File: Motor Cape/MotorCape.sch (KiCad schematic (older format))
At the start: 13 parts, among them J1 Conn_01x06, J2 Conn_01x06, J3 Conn_01x06, J4 Conn_01x06, J5 Conn_01x06, J6 Conn_01x06, J7 Conn_01x02, J8 Servo1, J9 Servo2, U1 MotorControl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

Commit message: Worked on wiring motor cape connections.
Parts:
- removed J5, J6: Conn_01x06, symbol Conn_01x06
- removed U3: MotorControl, symbol MotorControl
- added J5: Servo 3, symbol Conn_01x03
- added J6: Servo 4, symbol Conn_01x03
- J1: value Conn_01x06 -> Front Motor 1
- J2: value Conn_01x06 -> Front Motor 2
- J3: value Conn_01x06 -> Back Motor 1
- J4: value Conn_01x06 -> Back Motor 2
- J8: value Servo1 -> Servo 1
- J9: value Servo2 -> Servo 2
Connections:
- net labels added: GND
- net labels removed: +3.3V
- wire segments 36 -> 93
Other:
- moved on the sheet: J2, J3, J4, J7, J8, J9

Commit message: Changes made during meeting
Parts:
- removed J5: Servo 3, symbol Conn_01x03
- removed J6: Servo 4, symbol Conn_01x03
- removed U8: BoneHeaderP8, symbol BoneHeaderP8
- added ARD1: Arduino_Due_Shield, symbol Arduino_Due_Shield
- added J10: Servo2, Pin_Headers:Pin_Header_Angled_1x03_Pitch2.54mm, symbol Conn_01x03
- added J11: Servo1, Pin_Headers:Pin_Header_Angled_1x03_Pitch2.54mm, symbol Conn_01x03
- added J5, J6: Conn_01x06, Pin_Headers:Pin_Header_Angled_1x06_Pitch2.54mm, symbol Conn_01x06
- added U3: MotorControl, symbol MotorControl
- J1: value Front Motor 1 -> Conn_01x06; footprint (none) -> Pin_Headers:Pin_Header_Angled_1x06_Pitch2.54mm
- J2: value Front Motor 2 -> Conn_01x06; footprint (none) -> Pin_Headers:Pin_Header_Angled_1x06_Pitch2.54mm
- J3: value Back Motor 1 -> Conn_01x06; footprint (none) -> Pin_Headers:Pin_Header_Angled_1x06_Pitch2.54mm
- J4: value Back Motor 2 -> Conn_01x06; footprint (none) -> Pin_Headers:Pin_Header_Angled_1x06_Pitch2.54mm
- J8: value Servo 1 -> Servo4; footprint (none) -> Pin_Headers:Pin_Header_Angled_1x03_Pitch2.54mm
- J9: value Servo 2 -> Servo3; footprint (none) -> Pin_Headers:Pin_Header_Angled_1x03_Pitch2.54mm
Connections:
- net labels added: +3.3V
- net labels removed: GND
- wire segments 93 -> 44
- no-connect marks 10 -> 0
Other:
- note removed: "Quad Encoders\n"
- moved on the sheet: J2, J3, J4, J7, J8, J9

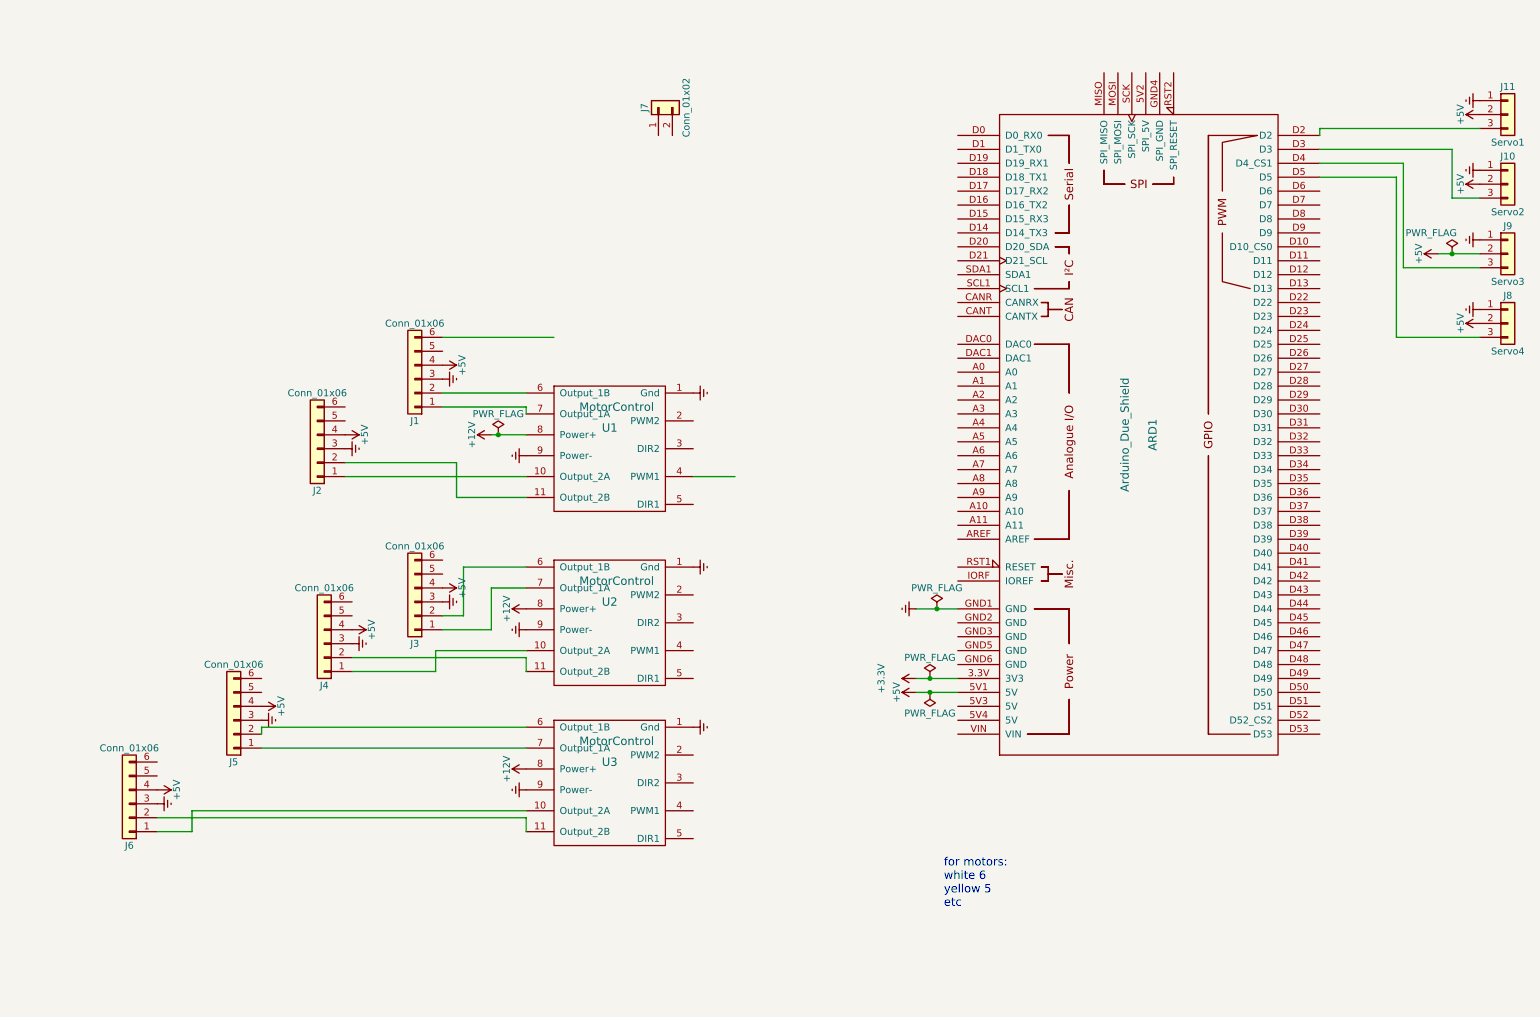
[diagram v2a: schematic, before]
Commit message: updated electrical connections. need to finish connectors on schematic.
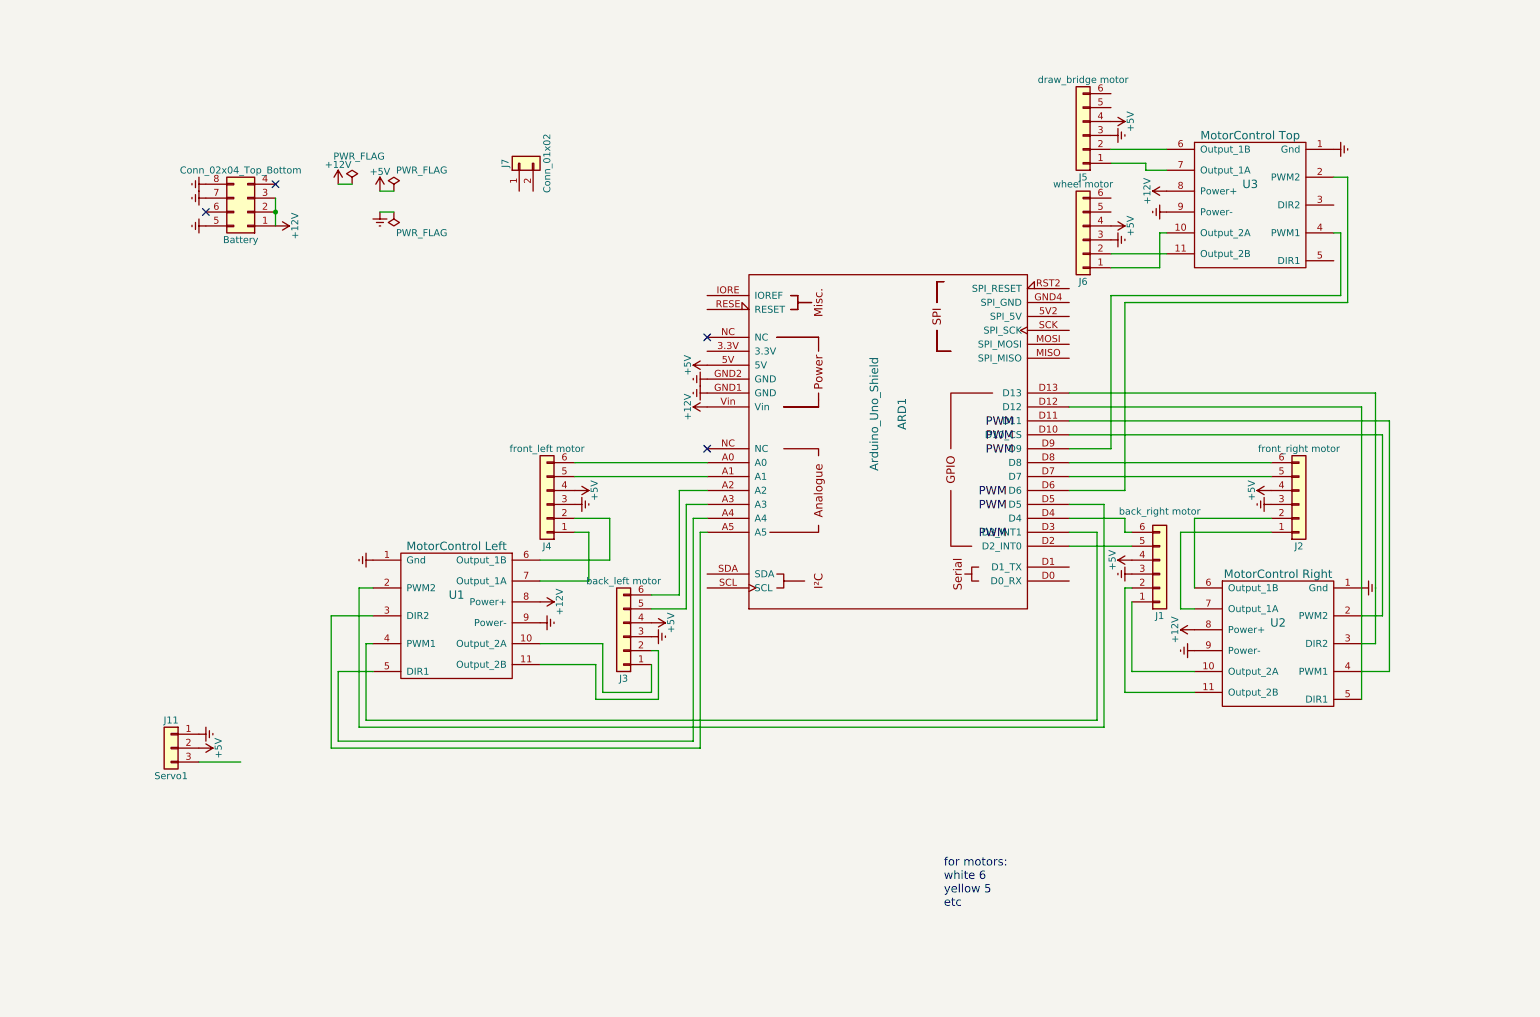
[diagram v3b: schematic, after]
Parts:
- removed ARD1: Arduino_Due_Shield, symbol Arduino_Due_Shield
- removed J10: Servo2, Pin_Headers:Pin_Header_Angled_1x03_Pitch2.54mm, symbol Conn_01x03
- removed J8: Servo4, Pin_Headers:Pin_Header_Angled_1x03_Pitch2.54mm, symbol Conn_01x03
- removed J9: Servo3, Pin_Headers:Pin_Header_Angled_1x03_Pitch2.54mm, symbol Conn_01x03
- added ARD1: Arduino_Uno_Shield, symbol Arduino_Uno_Shield
- added Battery: Conn_02x04_Top_Bottom, symbol Conn_02x04_Top_Bottom
- J1: value Conn_01x06 -> back_right motor
- J2: value Conn_01x06 -> front_right motor
- J3: value Conn_01x06 -> back_left motor
- J4: value Conn_01x06 -> front_left motor
- J5: value Conn_01x06 -> draw_bridge motor
- J6: value Conn_01x06 -> wheel motor
- U1: value MotorControl -> MotorControl Left
- U2: value MotorControl -> MotorControl Right
- U3: value MotorControl -> MotorControl Top
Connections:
- net labels added: PWM
- net labels removed: +3.3V
- wire segments 44 -> 94
- no-connect marks 0 -> 4
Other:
- moved on the sheet: J1, J11, J2, J3, J4, J5, J6, J7, U1, U2, U3

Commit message: updated labels
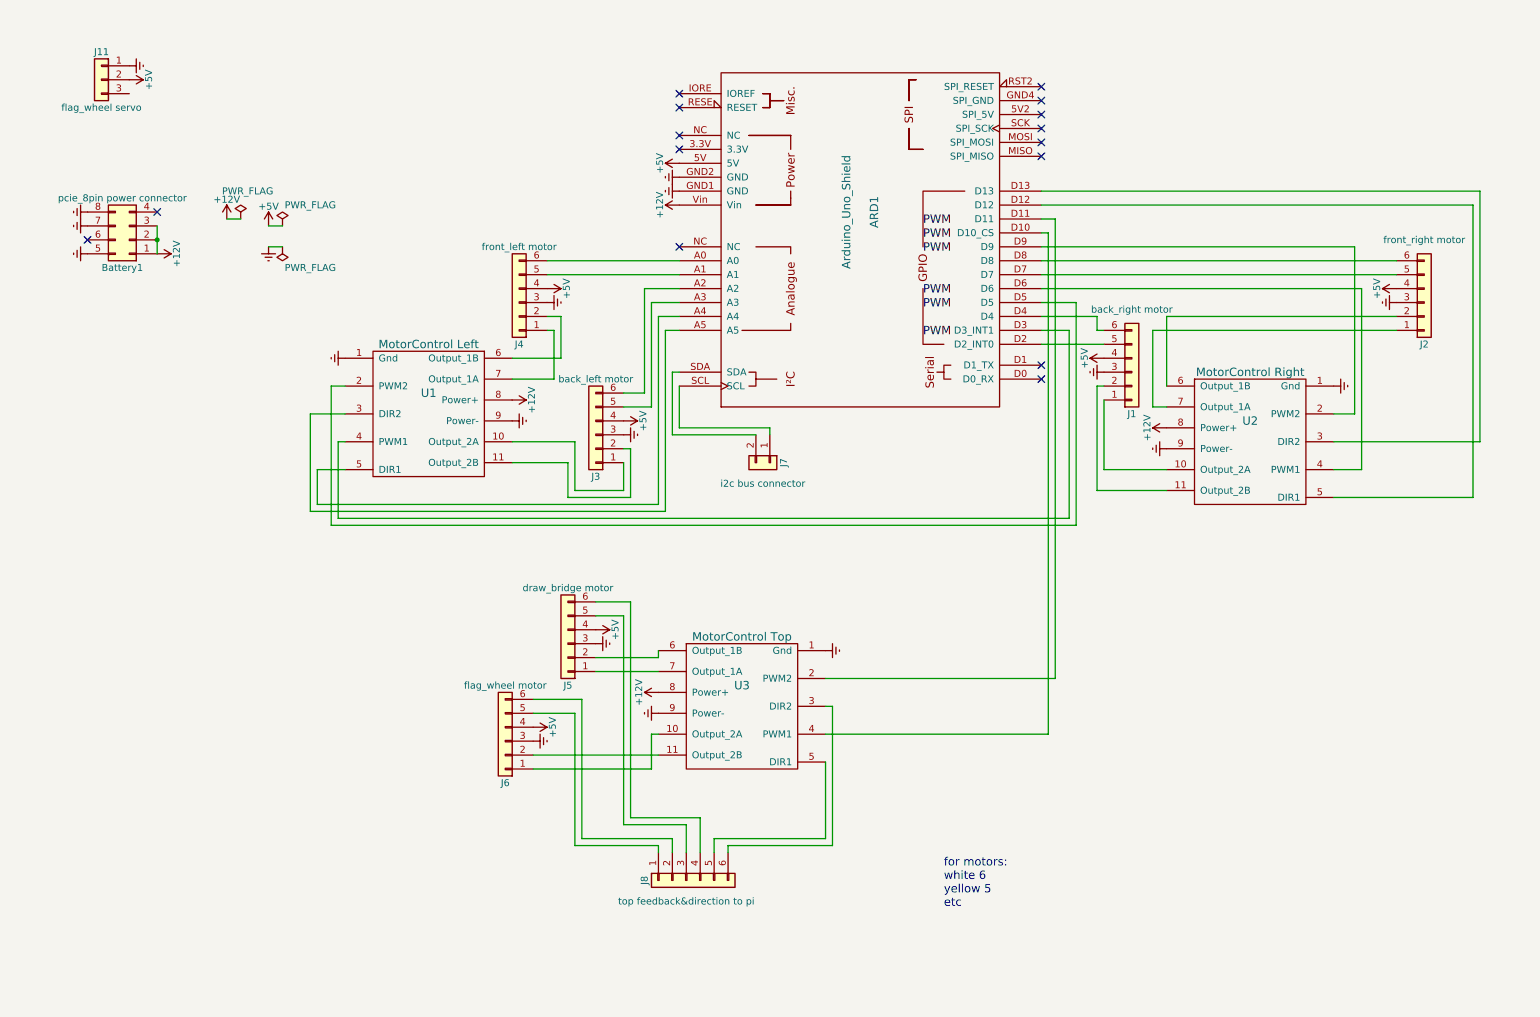
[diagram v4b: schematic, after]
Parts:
- added J8: top feedback&direction to pi, Pin_Headers:Pin_Header_Angled_1x06_Pitch2.54mm, symbol Conn_01x06
- Battery1: renamed from Battery; value Conn_02x04_Top_Bottom -> pcie_8pin power connector
- J11: value Servo1 -> flag_wheel servo
- J6: value wheel motor -> flag_wheel motor
- J7: value Conn_01x02 -> i2c bus connector
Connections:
- net at U2.2 (PWM2): now also ARD1.D9; no longer ARD1.D10 (D10_CS)
- net at U2.4 (PWM1): now also ARD1.D6; no longer ARD1.D11
- net at U3.2 (PWM2): now also ARD1.D11; no longer ARD1.D6
- net at U3.3 (DIR2): now also J8.6 (Pin_6)
- net at U3.4 (PWM1): now also ARD1.D10 (D10_CS); no longer ARD1.D9
- net at U3.5 (DIR1): now also J8.5 (Pin_5)
- net at J6.5 (Pin_5): now also J8.1 (Pin_1)
- net at J6.6 (Pin_6): now also J8.2 (Pin_2)
- net at J5.5 (Pin_5): now also J8.3 (Pin_3)
- net at J5.6 (Pin_6): now also J8.4 (Pin_4)
- net at J7.1 (Pin_1): now also ARD1.SCL
- net at J7.2 (Pin_2): now also ARD1.SDA
- no-connect marks 4 -> 15
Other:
- moved on the sheet: ARD1, Battery1, J1, J11, J2, J3, J4, J5, J6, J7, U1, U2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

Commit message: added level shifters and due and pi and labels
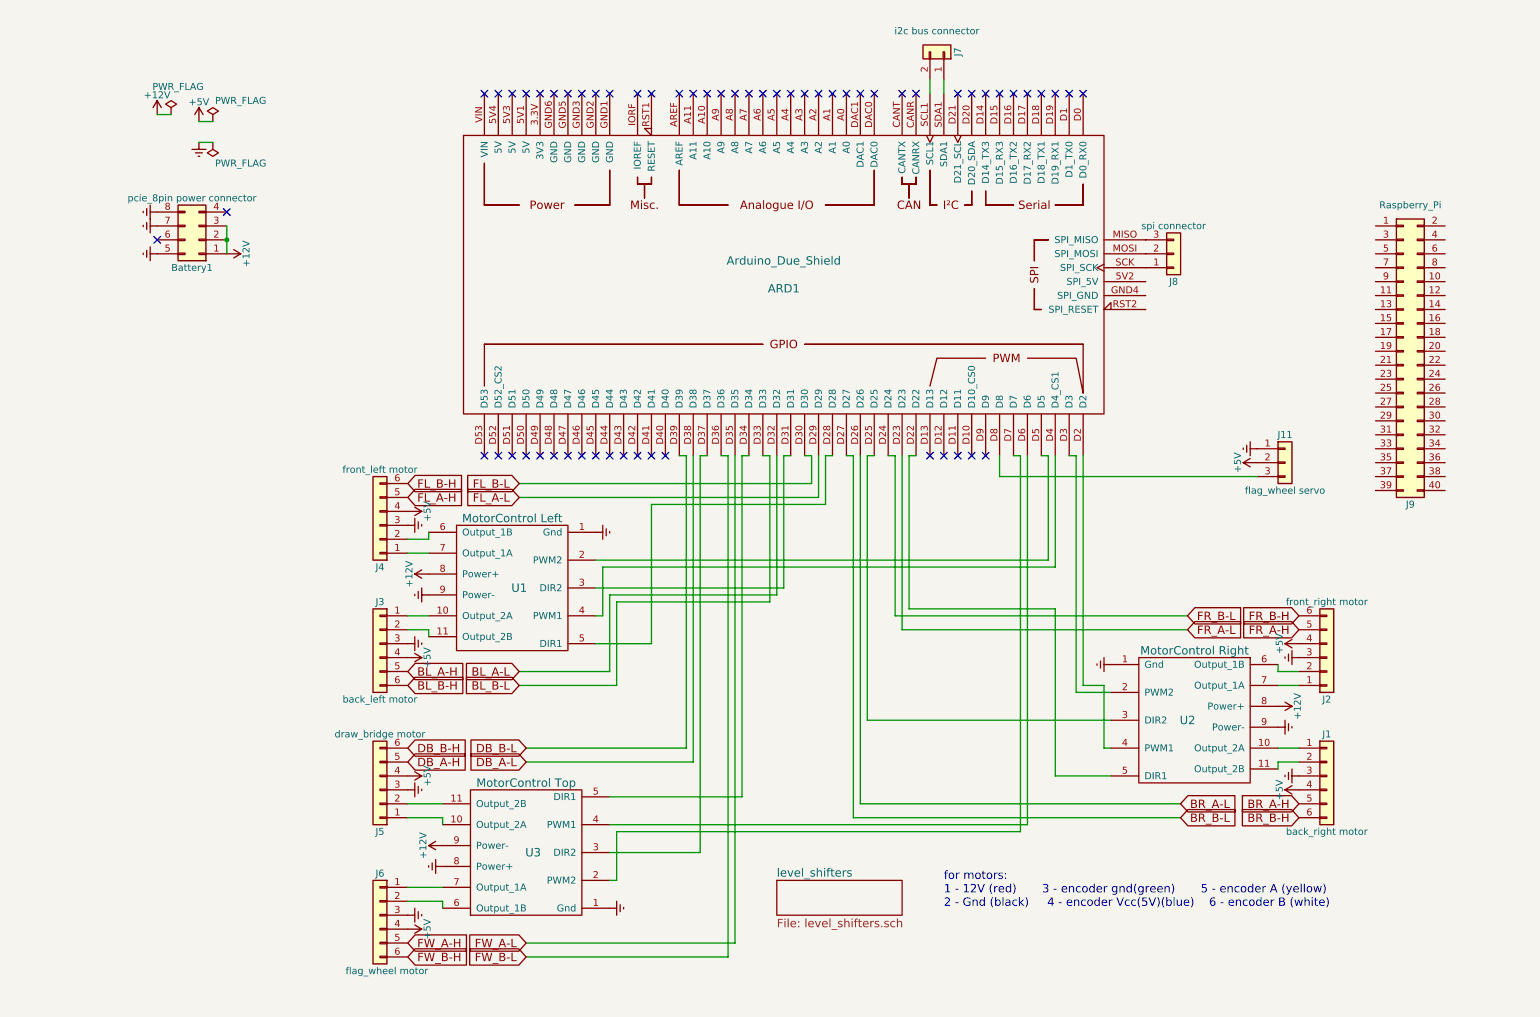
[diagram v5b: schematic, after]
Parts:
- removed ARD1: Arduino_Uno_Shield, symbol Arduino_Uno_Shield
- removed J8: top feedback&direction to pi, Pin_Headers:Pin_Header_Angled_1x06_Pitch2.54mm, symbol Conn_01x06
- added ARD1: Arduino_Due_Shield, symbol Arduino_Due_Shield
- added J8: spi connector, symbol Conn_01x03
- added J9: Raspberry_Pi, symbol Conn_02x20_Odd_Even
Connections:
- net +12V: now also U3.9 (Power-); no longer U3.8 (Power+)
- net Earth: now also U3.8 (Power+); no longer U3.9 (Power-)
- net at U2.2 (PWM2): now also ARD1.D3
- net at U2.3 (DIR2): now also ARD1.D25
- net at U2.4 (PWM1): now also ARD1.D2
- net at U2.5 (DIR1): now also ARD1.D22
- net at U1.2 (PWM2): now also ARD1.D5
- net at U1.3 (DIR2): now also ARD1.D31
- net at U1.4 (PWM1): now also ARD1.D4 (D4_CS1)
- net at U1.5 (DIR1): now also ARD1.D28
- net at U3.10 (Output_2A): now also J5.1 (Pin_1); no longer J6.1 (Pin_1)
- net at U3.11 (Output_2B): now also J5.2 (Pin_2); no longer J6.2 (Pin_2)
- net at U3.2 (PWM2): now also ARD1.D7
- net at U3.3 (DIR2): now also ARD1.D37
- net at U3.4 (PWM1): now also ARD1.D6
- net at U3.5 (DIR1): now also ARD1.D34
- net at U3.6 (Output_1B): now also J6.2 (Pin_2); no longer J5.2 (Pin_2)
- net at U3.7 (Output_1A): now also J6.1 (Pin_1); no longer J5.1 (Pin_1)
- net BR_A-H: now reaches J1.5 (Pin_5)
- net BR_B-H: now reaches J1.6 (Pin_6)
- net FR_A-H: now reaches J2.5 (Pin_5)
- net FR_B-H: now reaches J2.6 (Pin_6)
- net BL_A-H: now reaches J3.5 (Pin_5)
- net BL_B-H: now reaches J3.6 (Pin_6)
- net FL_A-H: now reaches J4.5 (Pin_5)
- net FL_B-H: now reaches J4.6 (Pin_6)
- net FW_A-H: now reaches J6.5 (Pin_5)
- net FW_B-H: now reaches J6.6 (Pin_6)
- net DB_A-H: now reaches J5.5 (Pin_5)
- net DB_B-H: now reaches J5.6 (Pin_6)
- net at J7.1 (Pin_1): now also ARD1.SDA1
- net at J7.2 (Pin_2): now also ARD1.SCL1
- net at J11.3 (Pin_3): now also ARD1.D8
- new net: ARD1.MISO (SPI_MISO), J8.3 (Pin_3)
- new net: ARD1.MOSI (SPI_MOSI), J8.2 (Pin_2)
- new net: ARD1.SCK (SPI_SCK), J8.1 (Pin_1)
- new net BL_A-L: ARD1.D32
- new net BL_B-L: ARD1.D33
- new net BR_A-L: ARD1.D26
- new net BR_B-L: ARD1.D27
- new net DB_A-L: ARD1.D38
- new net DB_B-L: ARD1.D39
- new net FL_A-L: ARD1.D29
- new net FL_B-L: ARD1.D30
- new net FR_A-L: ARD1.D23
- new net FR_B-L: ARD1.D24
- new net FW_A-L: ARD1.D35
- new net FW_B-L: ARD1.D36
- no-connect marks 15 -> 60
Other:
- note added: "for motors: \n1 - 12V (red) 3 - encoder gnd(green) 5 - encoder A (yellow)\n2 - Gnd (black) 4 - encoder Vcc(5V)(blue) 6 - encoder B (white)\n"
- note removed: "for motors:\nwhite 6\nyellow 5\netc\n"
- moved on the sheet: Battery1, J1, J11, J2, J3, J4, J5, J6, J7, U1, U2, U3

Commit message: fixed drc errors, added serial comm between pi & due, now just need to choose power connector & fuse
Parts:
- removed J8: spi connector, symbol Conn_01x03
- removed J9: Raspberry_Pi, symbol Conn_02x20_Odd_Even
- added F1: Fuse, symbol Fuse
- added J9: Raspberry_Pi_2_3, Pin_Headers:Pin_Header_Straight_2x20, symbol Raspberry_Pi_2_3
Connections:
- net +5V: now also ARD1.5V2 (SPI_5V)
- net Earth: now also ARD1.GND4 (SPI_GND); no longer Battery1.5 (Pin_5), Battery1.7 (Pin_7), Battery1.8 (Pin_8), U1.9 (Power-), U2.9 (Power-), U3.8 (Power+)
- net SCL: now reaches J7.1 (Pin_1)
- net SCL: now also ARD1.SCL1, J9.5 ((SCL1)_GPIO3); no longer ARD1.SDA1
- net SDA: now reaches J7.2 (Pin_2)
- net SDA: now also ARD1.SDA1, J9.3 ((SDA1)_GPIO2); no longer ARD1.SCL1
- net FROM_Pi: now reaches ARD1.D0 (D0_RX0)
- net FROM_Pi: now also J9.8 ((TXD0)_GPIO14)
- net TO_Pi: now reaches ARD1.D1 (D1_TX0)
- net TO_Pi: now also J9.10 ((RXD0)_GPIO15)
- net at ARD1.MISO (SPI_MISO): now also J9.21 ((SPI_MISO)_GPIO9)
- net at ARD1.MOSI (SPI_MOSI): now also J9.19 ((SPI_MOSI)_GPIO10)
- net at ARD1.RST2 (SPI_RESET): now also J9.24 ((~SPI_CE0~)_GPIO8)
- net at ARD1.SCK (SPI_SCK): now also J9.23 ((SPI_SCLK)_GPIO11)
- net +12V renamed MOTOR_PWR
- net MOTOR_PWR: now also F1.1; no longer Battery1.1 (Pin_1), Battery1.2 (Pin_2), Battery1.3 (Pin_3)
- new net MOTOR_GND: U1.9 (Power-), U2.9 (Power-), U3.8 (Power+)
- no-connect marks 60 -> 88
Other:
- note added: "MOTOR_PWR=12V\nfor motors:\n1 - 12V (red) 3 - encoder gnd(green) 5 - encoder A (yellow)\n2 - Gnd (black) 4 - encoder Vcc(5V)(blue) 6 - encoder B (white)\n"
- note removed: "for motors: \n1 - 12V (red) 3 - encoder gnd(green) 5 - encoder A (yellow)\n2 - Gnd (black) 4 - encoder Vcc(5V)(blue) 6 - encoder B (white)\n"
- moved on the sheet: Battery1, J11, J7
